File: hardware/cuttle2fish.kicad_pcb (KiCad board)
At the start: 2 copper layers, 22.4 x 47.3 mm, 26 parts, among them J2 CONN_01X05, J3 CONN_01x05, SW1 SW_SPST, U1 LP2985-3.3, U2 STM32F103R(8-B)Tx, U3 APA102-2020, U4 APA102-2020, U5 USB_PCB, Y1 10pF

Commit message: routing attempt #1 (bad)
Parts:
- moved C10 2.00 mm to (114.2, 62.2)
- moved R1 2.00 mm to (110.5, 62.5)
- moved R2 2.00 mm to (112.5, 62.5)
- moved C11 1.75 mm to (116.2, 62.2)
- turned Y1 to 0 degrees
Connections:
- C3 pad 1: Net-(C3-Pad1) -> +3V3
- C4 pad 1: Net-(C4-Pad1) -> +3V3
- C5 pad 1: Net-(C5-Pad1) -> +3V3
- C6 pad 1: Net-(C6-Pad1) -> +3V3
- J3 pad 3: /PB0 -> /PB1
- J3 pad 4: /PB1 -> /PB0
- U2 pad 13: Net-(C6-Pad1) -> +3V3
- U2 pad 32: Net-(C3-Pad1) -> +3V3
- U2 pad 48: Net-(C4-Pad1) -> +3V3
- U2 pad 64: Net-(C5-Pad1) -> +3V3
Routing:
- net +3V3: track 0.00 -> 75.1 mm, vias 0 -> 10
- net GND: track 0.00 -> 51.3 mm, vias 0 -> 12
- net /SPI1_SCK: track 0.00 -> 33.9 mm, vias 0 -> 2
- net /SPI1_MOSI: track 0.00 -> 31.5 mm, vias 0 -> 2
- net /LED: track 0.00 -> 29.9 mm, vias 0 -> 2
- net /USART1_TX: track 0.00 -> 25.3 mm, vias 0 -> 2
- net /SWDIO: track 0.00 -> 25.3 mm
- net /BUTTON: track 0.00 -> 24.0 mm, vias 0 -> 2
- net /SWCLK: track 0.00 -> 23.1 mm, vias 0 -> 2
- net /USART1_RX: track 0.00 -> 20.8 mm, vias 0 -> 2
- net /PB1: track 0.00 -> 16.0 mm
- net /RESET: track 0.00 -> 14.4 mm
- net /PB0: track 0.00 -> 12.7 mm
- net Net-(C10-Pad1): track 0.00 -> 7.27 mm
- net Net-(C11-Pad1): track 0.00 -> 7.25 mm
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- added copper zone on F.Cu, net +3V3
- added copper zone on B.Cu, net GND

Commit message: layout v2!
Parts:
- turned C4 to 180 degrees
- turned C9 to 180 degrees
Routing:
- net +3V3: track 75.1 -> 11.8 mm, vias 10 -> 0
- net /LED: track 29.9 -> 17.4 mm, vias 2 -> 0
- net /USART1_RX: track 20.8 -> 33.1 mm
- net /PB0: track 12.7 -> 21.7 mm, vias 0 -> 2
- net GND: track 51.3 -> 59.7 mm, vias 12 -> 13
- net /SPI1_SCK: track 33.9 -> 28.5 mm
- net /USB_DP: track 15.0 -> 12.1 mm, vias 2 -> 0
- net /SPI1_MOSI: track 31.5 -> 28.9 mm
- net /SWDIO: track 25.3 -> 23.4 mm
- net /USART1_TX: track 25.3 -> 26.8 mm
- net /PB1: track 16.0 -> 14.8 mm, vias 0 -> 2
- net /SWCLK: track 23.1 -> 22.1 mm
- net /RESET: track 14.4 -> 14.9 mm, vias 0 -> 2
- net +5V: track 15.4 -> 15.7 mm, vias 0 -> 2
- net /USB_DM: track 13.2 -> 13.0 mm, vias 2 -> 0
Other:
- rule trace_min: 0.2 -> 0.16

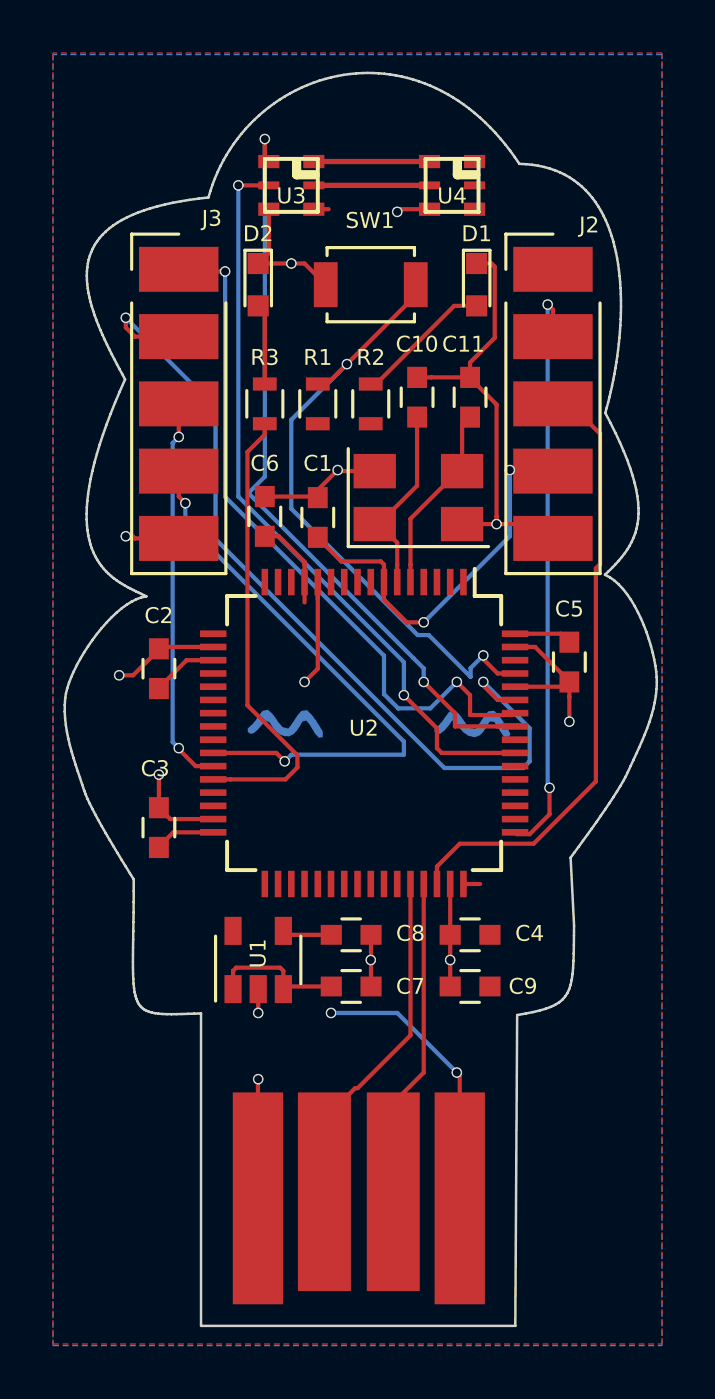
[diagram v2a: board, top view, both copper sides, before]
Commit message: tweak layout, expose eyes in outline
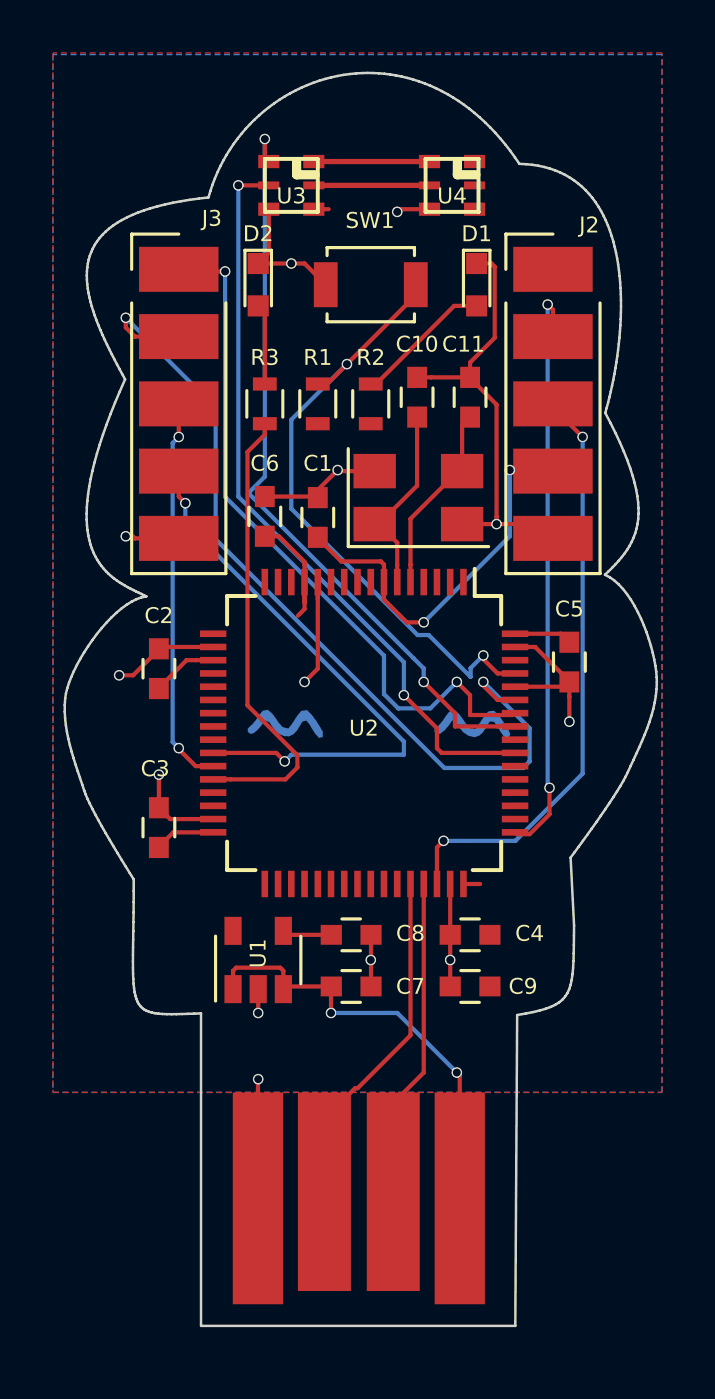
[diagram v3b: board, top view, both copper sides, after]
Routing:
- net +3V3: track 11.8 -> 13.1 mm
- net +5V: track 15.7 -> 16.7 mm
- net /SWDIO: track 23.4 -> 23.1 mm, vias 0 -> 2

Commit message: rev A gerbers
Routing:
- net GND: track 59.7 -> 60.4 mm, vias 13 -> 14
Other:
- board text added: "cuttl2fish ~tahnok~ rev A"
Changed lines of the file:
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@@
   (general
     (thickness 1.6)
-    (drawings 0)
-    (tracks 269)
+    (drawings 1)
+    (tracks 274)
     (zones 0)
     (modules 26)
@@
     (visible_elements 7FFFFFFF)
     (pcbplotparams
-      (layerselection 0x010fc_ffffffff)
-      (usegerberextensions false)
+      (layerselection 0x010f0_ffffffff)
+      (usegerberextensions true)
       (usegerberattributes false)
       (usegerberadvancedattributes false)
@@
       (plotinvisibletext false)
       (padsonsilk false)
-      (subtractmaskfromsilk false)
+      (subtractmaskfromsilk true)
       (outputformat 1)
       (mirror false)
-      (drillshape 1)
+      (drillshape 0)
       (scaleselection 1)
-      (outputdirectory ""))
+      (outputdirectory "rev_a/gerbers/"))
   )
   (net 0 "")
@@
     )
   )
+  (gr_text "cuttl2fish\n~tahnok~\nrev A" (at 112.25 87.25) (layer B.SilkS)
+    (effects (font (size 0.4 0.4) (thickness 0.05)) (justify mirror))
+  )
   (via (at 108.25 88) (size 0.4) (drill 0.3) (layers F.Cu B.Cu) (net 1))
   (segment (start 108.24 92.5) (end 108.24 88.01) (width 0.16) (layer F.Cu) (net 1))
@@
   (segment (start 110.5 69.23) (end 110.5 72.5) (width 0.16) (layer F.Cu) (net 1))
   (segment (start 110.5 72.5) (end 110 73) (width 0.16) (layer F.Cu) (net 1))
+  (via (at 108 55.25) (size 0.4) (drill 0.3) (layers F.Cu B.Cu) (net 1))
+  (segment (start 108.65 55.15) (end 108.1 55.15) (width 0.16) (layer F.Cu) (net 1))
+  (segment (start 108.1 55.15) (end 108 55.25) (width 0.16) (layer F.Cu) (net 1))
   (segment (start 113 68.57) (end 113 69.23) (width 0.16) (layer F.Cu) (net 2))
   (segment (start 112.879999 68.449999) (end 113 68.57) (width 0.16) (layer F.Cu) (net 2))
@@
   (segment (start 114.5 87.75) (end 114.5 80.63) (width 0.16) (layer F.Cu) (net 49))
   (segment (start 113.5 88.75) (end 114.5 87.75) (width 0.16) (layer F.Cu) (net 49))
-  (via (at 107.5 54.25) (size 0.4) (drill 0.3) (layers F.Cu B.Cu) (net 55))
-  (segment (start 108.65 54.25) (end 107.5 54.25) (width 0.16) (layer F.Cu) (net 55))
-  (segment (start 107.5 54.25) (end 107.5 66) (width 0.16) (layer B.Cu) (net 55))
+  (segment (start 107.5 56.25) (end 107.5 66) (width 0.16) (layer B.Cu) (net 55))
   (segment (start 117.18 75.68) (end 117.95 75.68) (width 0.16) (layer F.Cu) (net 55))
   (segment (start 117.18 75.68) (end 115.18 75.68) (width 0.16) (layer F.Cu) (net 55))
@@
   (segment (start 113.75 72.25) (end 113.75 73.5) (width 0.16) (layer B.Cu) (net 55))
   (segment (start 107.5 66) (end 113.75 72.25) (width 0.16) (layer B.Cu) (net 55))
+  (via (at 107.5 56.25) (size 0.4) (drill 0.3) (layers F.Cu B.Cu) (net 55))
+  (segment (start 108.09 54.25) (end 108.65 54.25) (width 0.16) (layer F.Cu) (net 55))
+  (segment (start 107.5 54.84) (end 108.09 54.25) (width 0.16) (layer F.Cu) (net 55))
+  (segment (start 107.5 56.25) (end 107.5 54.84) (width 0.16) (layer F.Cu) (net 55))
   (segment (start 117.29 74.68) (end 117.95 74.68) (width 0.16) (layer F.Cu) (net 57))
   (segment (start 117.29 74.68) (end 115.68 74.68) (width 0.16) (layer F.Cu) (net 57))
